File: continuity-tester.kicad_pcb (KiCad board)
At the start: 2 copper layers, 60 x 33 mm, 29 parts, among them J1 Conn_01x01_Pin, J2 Conn_01x01_Pin, J3 Conn_01x01_Pin, J4 Conn_01x01_Pin, Q1 2N3906, Q2 2N3904, Q3 2N3904, U1 MCP6022

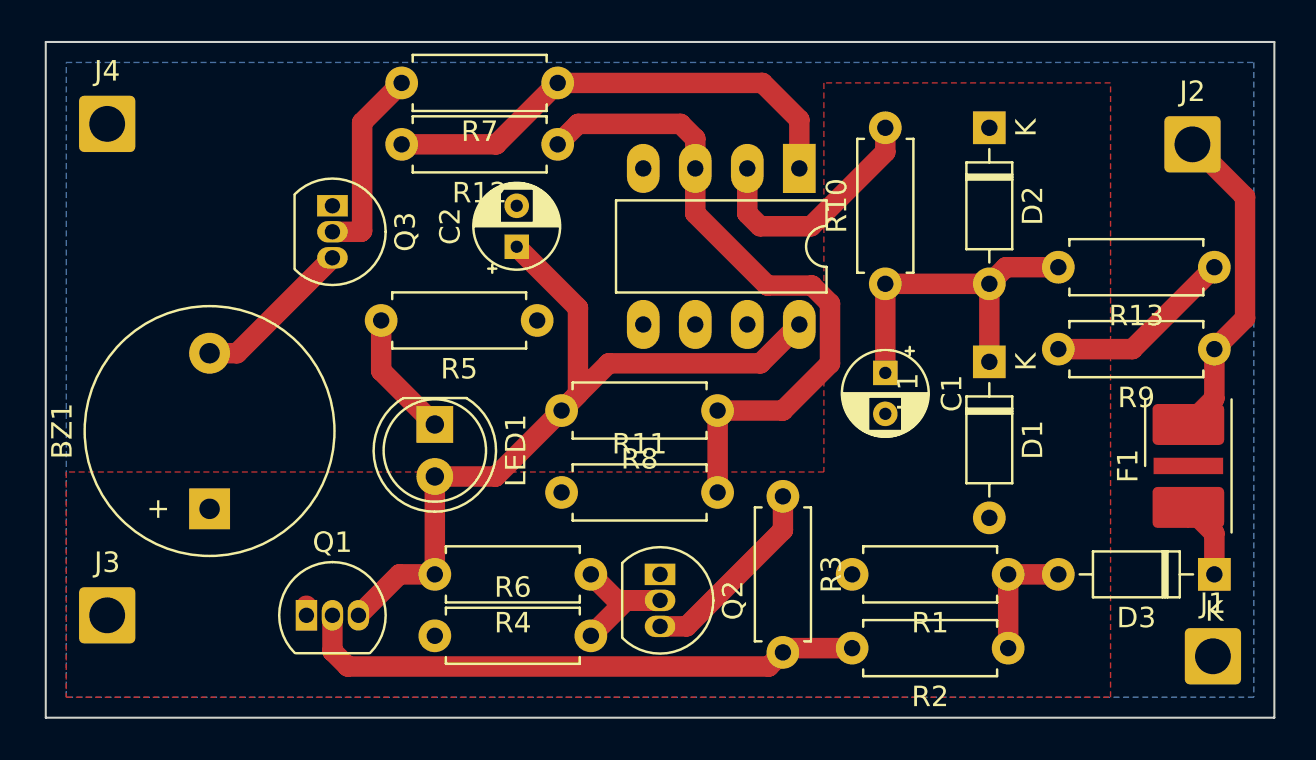
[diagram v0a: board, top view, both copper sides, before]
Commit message: added board dimensions to silkscreen
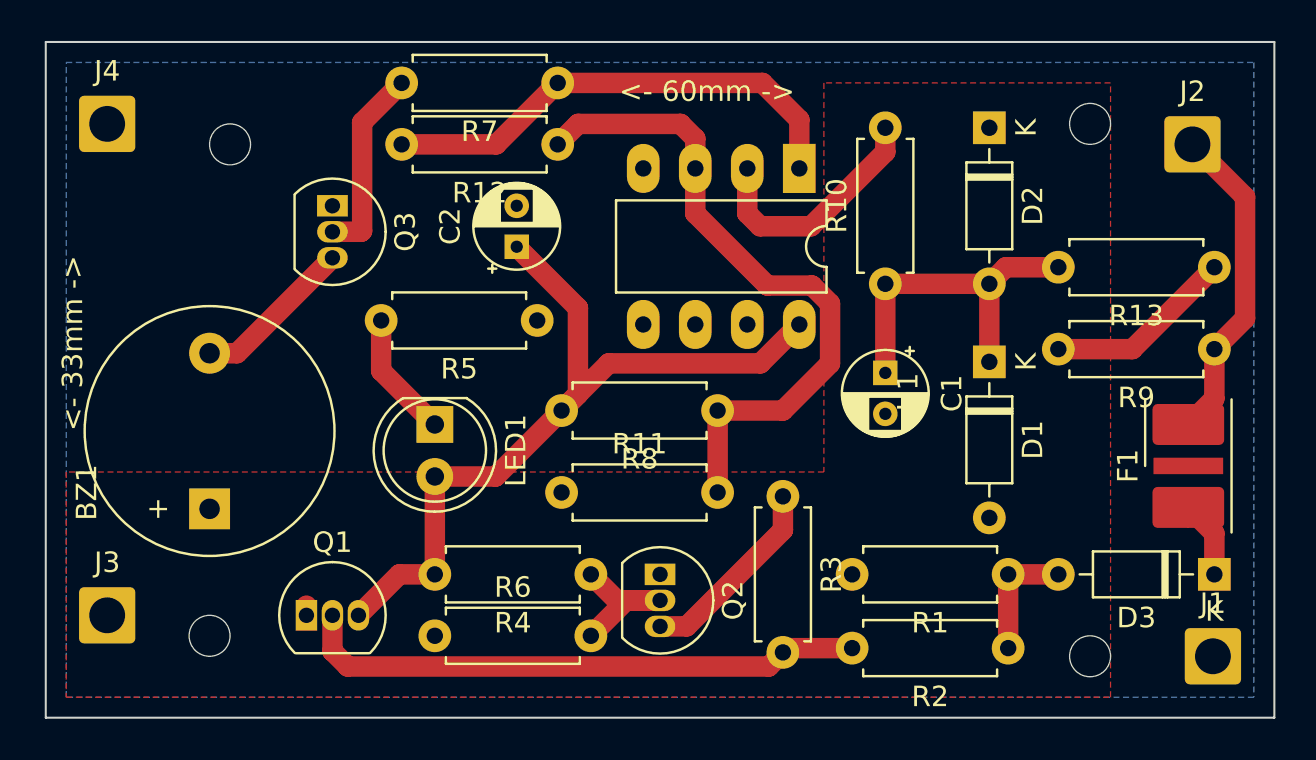
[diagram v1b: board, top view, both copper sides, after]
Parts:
- added H1: MountingHole_Pad, MountingHole:MountingHole_2mm, F.Cu at (131.0, 93.0)
- added H2: MountingHole_Pad, MountingHole:MountingHole_2mm, F.Cu at (130.0, 117.0)
- added H3: MountingHole_Pad, MountingHole:MountingHole_2mm, F.Cu at (173.0, 92.0)
- added H4: MountingHole_Pad, MountingHole:MountingHole_2mm, F.Cu at (173.0, 118.0)
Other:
- board text added: "<- 33mm ->"
- board text added: "<- 60mm ->"
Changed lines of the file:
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@@
     )
+  )
+  (footprint "MountingHole:MountingHole_2mm" (layer "F.Cu")
+    (at 173 118)
+    (descr "Mounting Hole 2mm, no annular")
+    (tags "mounting hole 2mm no annular")
+    (property "Sheetfile" "continuity-tester.kicad_sch")
+    (property "Sheetname" "")
+    (property "ki_description" "Mounting Hole with connection")
+    (property "ki_keywords" "mounting hole")
+    (attr exclude_from_pos_files)
+    (fp_text reference "H4" (at 0 -3.2) (layer "F.SilkS") hide
+        (effects (font (size 1 1) (thickness 0.15)))
+    )
+    (fp_text value "MountingHole_Pad" (at 0 3.1) (layer "F.Fab")
+        (effects (font (size 1 1) (thickness 0.15)))
+    )
+    (fp_text user "${REFERENCE}" (at 0 0) (layer "F.Fab")
+        (effects (font (size 1 1) (thickness 0.15)))
+    )
+    (fp_circle (center 0 0) (end 2 0)
+      (stroke (width 0.15) (type solid)) (fill none) (layer "Cmts.User"))
+    (fp_circle (center 0 0) (end 2.25 0)
+      (stroke (width 0.05) (type solid)) (fill none) (layer "F.CrtYd"))
+    (pad "" np_thru_hole circle (at 0 0) (size 2 2) (drill 2) (layers "*.Cu" "*.Mask"))
   )
   (footprint "Fuse:Fuse_Bourns_TBU-CA" (layer "F.Cu")
@@
     )
   )
+  (footprint "MountingHole:MountingHole_2mm" (layer "F.Cu")
+    (at 173 92)
+    (descr "Mounting Hole 2mm, no annular")
+    (tags "mounting hole 2mm no annular")
+    (property "Sheetfile" "continuity-tester.kicad_sch")
+    (property "Sheetname" "")
+    (property "ki_description" "Mounting Hole with connection")
+    (property "ki_keywords" "mounting hole")
+    (attr exclude_from_pos_files)
+    (fp_text reference "H3" (at 0 -3.2) (layer "F.SilkS") hide
+        (effects (font (size 1 1) (thickness 0.15)))
+    )
+    (fp_text value "MountingHole_Pad" (at 0 3.1) (layer "F.Fab")
+        (effects (font (size 1 1) (thickness 0.15)))
+    )
+    (fp_text user "${REFERENCE}" (at 0 0) (layer "F.Fab")
+        (effects (font (size 1 1) (thickness 0.15)))
+    )
+    (fp_circle (center 0 0) (end 2 0)
+      (stroke (width 0.15) (type solid)) (fill none) (layer "Cmts.User"))
+    (fp_circle (center 0 0) (end 2.25 0)
+      (stroke (width 0.05) (type solid)) (fill none) (layer "F.CrtYd"))
+    (pad "" np_thru_hole circle (at 0 0) (size 2 2) (drill 2) (layers "*.Cu" "*.Mask"))
+  )
   (footprint "Capacitor_THT:CP_Radial_D4.0mm_P2.00mm" (layer "F.Cu")
     (at 145 98 90)
@@
     (property "ki_keywords" "quartz resonator ceramic")
     (attr through_hole)
-    (fp_text reference "BZ1" (at 3.8 -7.2 90) (layer "F.SilkS")
+    (fp_text reference "BZ1" (at 0.8 -6 90) (layer "F.SilkS")
         (effects (font (size 1 1) (thickness 0.15)))
     )
@@
     )
   )
+  (footprint "MountingHole:MountingHole_2mm" (layer "F.Cu")
+    (at 130 117)
+    (descr "Mounting Hole 2mm, no annular")
+    (tags "mounting hole 2mm no annular")
+    (property "Sheetfile" "continuity-tester.kicad_sch")
+    (property "Sheetname" "")
+    (property "ki_description" "Mounting Hole with connection")
+    (property "ki_keywords" "mounting hole")
+    (attr exclude_from_pos_files)
+    (fp_text reference "H2" (at 0 -3.2) (layer "F.SilkS") hide
+        (effects (font (size 1 1) (thickness 0.15)))
+    )
+    (fp_text value "MountingHole_Pad" (at 0 3.1) (layer "F.Fab")
+        (effects (font (size 1 1) (thickness 0.15)))
+    )
+    (fp_text user "${REFERENCE}" (at 0 0) (layer "F.Fab")
+        (effects (font (size 1 1) (thickness 0.15)))
+    )
+    (fp_circle (center 0 0) (end 2 0)
+      (stroke (width 0.15) (type solid)) (fill none) (layer "Cmts.User"))
+    (fp_circle (center 0 0) (end 2.25 0)
+      (stroke (width 0.05) (type solid)) (fill none) (layer "F.CrtYd"))
+    (pad "" np_thru_hole circle (at 0 0) (size 2 2) (drill 2) (layers "*.Cu" "*.Mask"))
+  )
   (footprint "LED_THT:LED_D5.0mm" (layer "F.Cu")
     (at 141 106.68 -90)
@@
     )
   )
+  (footprint "MountingHole:MountingHole_2mm" (layer "F.Cu")
+    (at 131 93)
+    (descr "Mounting Hole 2mm, no annular")
+    (tags "mounting hole 2mm no annular")
+    (property "Sheetfile" "continuity-tester.kicad_sch")
+    (property "Sheetname" "")
+    (property "ki_description" "Mounting Hole with connection")
+    (property "ki_keywords" "mounting hole")
+    (attr exclude_from_pos_files)
+    (fp_text reference "H1" (at 0 -3.2) (layer "F.SilkS") hide
+        (effects (font (size 1 1) (thickness 0.15)))
+    )
+    (fp_text value "MountingHole_Pad" (at 0 3.1) (layer "F.Fab")
+        (effects (font (size 1 1) (thickness 0.15)))
+    )
+    (fp_text user "${REFERENCE}" (at 0 0) (layer "F.Fab")
+        (effects (font (size 1 1) (thickness 0.15)))
+    )
+    (fp_circle (center 0 0) (end 2 0)
+      (stroke (width 0.15) (type solid)) (fill none) (layer "Cmts.User"))
+    (fp_circle (center 0 0) (end 2.25 0)
+      (stroke (width 0.05) (type solid)) (fill none) (layer "F.CrtYd"))
+    (pad "" np_thru_hole circle (at 0 0) (size 2 2) (drill 2) (layers "*.Cu" "*.Mask"))
+  )
   (footprint "Connector_Wire:SolderWire-1sqmm_1x01_D1.4mm_OD2.7mm" (layer "F.Cu")
     (at 179 118)
@@
   (gr_rect (start 122 88) (end 182 121)
     (stroke (width 0.1) (type default)) (fill none) (layer "Edge.Cuts"))
+  (gr_text "<- 60mm ->" (at 150 91) (layer "F.SilkS")
+    (effects (font (size 1 1) (thickness 0.15)) (justify left bottom))
+  )
+  (gr_text "<- 33mm ->" (at 123.9 107 90) (layer "F.SilkS")
+    (effects (font (size 1 1) (thickness 0.15)) (justify left bottom))
+  )
   (segment (start 130 111) (end 130 110.8) (width 0.25) (layer "F.Cu") (net 1))
   (segment (start 134.73 116) (end 134.73 115.53) (width 1) (layer "F.Cu") (net 1))

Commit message: Silkscreen
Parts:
- moved H1 1.00 mm to (130.0, 93.0)
- moved H2 1.00 mm to (130.0, 118.0)
- moved H3 1.00 mm to (173.0, 93.0)
- renumbered J4 to GND, J1 to PRB_GND, J2 to PROBE, J3 to VCC/3V
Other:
- board text added: "M2"
- board text added: "|<- 33mm ->| <- 25mm ->"
- board text added: "|<- 60mm ->| <- 43mm ->"
- board text removed: "<- 33mm ->"
- board text removed: "<- 60mm ->"

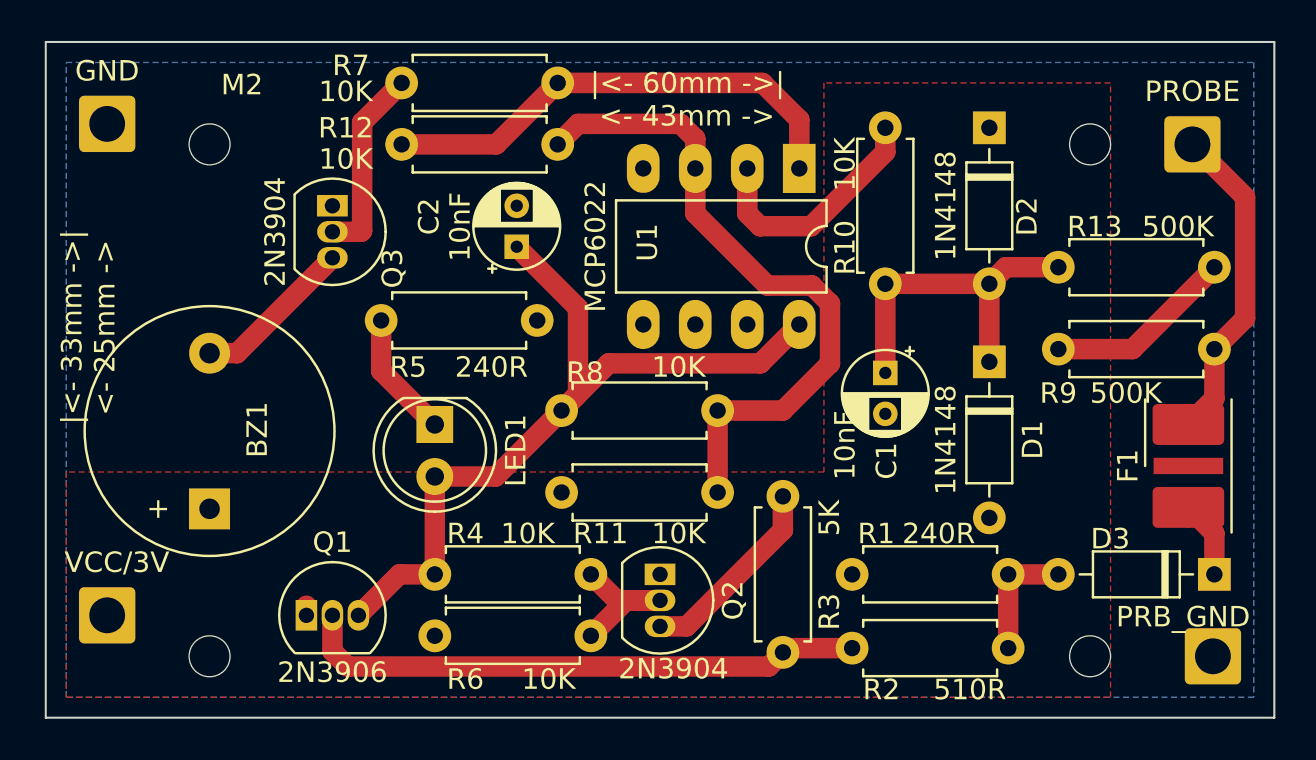
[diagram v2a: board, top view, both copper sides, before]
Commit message: Nicer planes
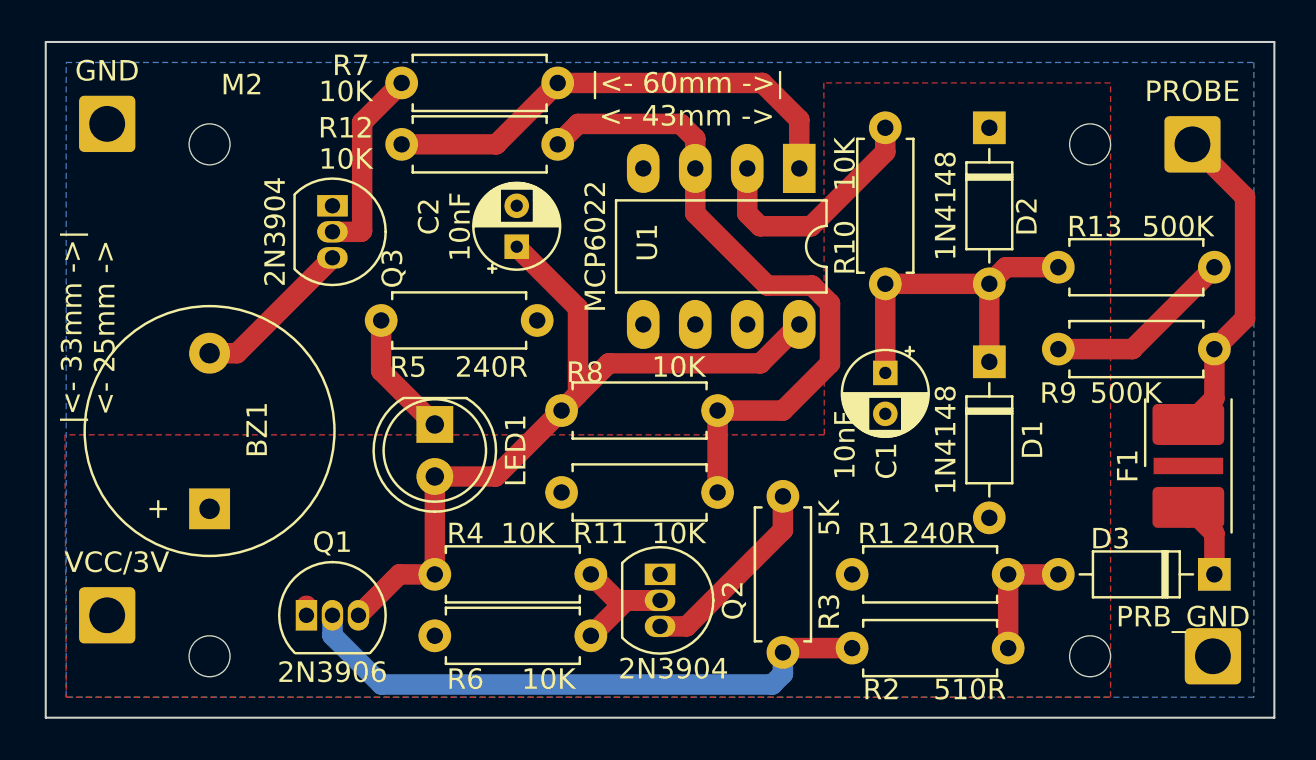
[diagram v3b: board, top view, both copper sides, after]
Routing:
- net Net-(Q1-B): track 27.8 -> 28.7 mm
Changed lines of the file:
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@@
   (segment (start 177.9435 93.0564) (end 177.8889 93.111) (width 0.25) (layer "B.Cu") (net 9))
   (segment (start 178 93) (end 177.9435 93.0564) (width 0.25) (layer "B.Cu") (net 9))
-  (segment (start 136 116) (end 136 117.75) (width 1) (layer "F.Cu") (net 10))
   (segment (start 161.38 117.602) (end 158.208 117.602) (width 1) (layer "F.Cu") (net 10))
-  (segment (start 136 117.75) (end 136.75 118.5) (width 1) (layer "F.Cu") (net 10))
   (segment (start 158.208 117.602) (end 158 117.81) (width 1) (layer "F.Cu") (net 10))
-  (segment (start 136.75 118.5) (end 157.31 118.5) (width 1) (layer "F.Cu") (net 10))
-  (segment (start 157.31 118.5) (end 158 117.81) (width 1) (layer "F.Cu") (net 10))
+  (segment (start 136 116.984) (end 138.396 119.38) (width 1) (layer "B.Cu") (net 10))
+  (segment (start 136 116) (end 136 116.984) (width 1) (layer "B.Cu") (net 10))
+  (segment (start 158 118.86) (end 158 117.81) (width 1) (layer "B.Cu") (net 10))
+  (segment (start 138.396 119.38) (end 157.48 119.38) (width 1) (layer "B.Cu") (net 10))
+  (segment (start 157.48 119.38) (end 158 118.86) (width 1) (layer "B.Cu") (net 10))
   (segment (start 158 111.84) (end 158 110.19) (width 1) (layer "F.Cu") (net 11))
   (segment (start 153.3 116.54) (end 158 111.84) (width 1) (layer "F.Cu") (net 11))
@@
     (connect_pads (clearance 0.5))
     (min_thickness 0.25) (filled_areas_thickness no)
-    (fill yes (thermal_gap 0.5) (thermal_bridge_width 0.5))
+    (fill yes (thermal_gap 0.5) (thermal_bridge_width 0.5) (smoothing fillet) (radius 2))
     (polygon
       (pts
@@
         (xy 174 90)
         (xy 160 90)
-        (xy 160 109)
-        (xy 123 109)
+        (xy 160.02 107.188)
+        (xy 122.936 107.188)
       )
     )
@@
     (connect_pads (clearance 0.5))
     (min_thickness 0.25) (filled_areas_thickness no)
-    (fill yes (thermal_gap 0.5) (thermal_bridge_width 0.5))
+    (fill yes (thermal_gap 0.5) (thermal_bridge_width 0.5) (smoothing fillet) (radius 2))
     (polygon
       (pts
